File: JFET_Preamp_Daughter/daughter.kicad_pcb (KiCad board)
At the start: 2 copper layers, 80 x 120 mm, 90 parts, among them J101 Conn_01x02, J102 Conn_01x08_Socket, J201 XLR3, J301 XLR3, J401 XLR3, J501 XLR3, Q201 2SK209, Q202 2SK209, Q203 2SK209, Q301 2SK209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

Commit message: finish draft of mother/daughter sch and start routing, reconcile libraries and missing footprints
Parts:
- removed C201, C202, C203, C301, C302, C303, C401, C402, C403, C501, C502, C503: 220p, Capacitor_SMD:C_0603_1608Metric
- removed C204, C205, C304, C305, C404, C405, C504, C505: 10u, Capacitor_SMD:C_0805_2012Metric
- removed D102: LED, LED_SMD:LED_0603_1608Metric
- removed D201, D202, D301, D302, D401, D402, D501, D502: D_TVS, MMBZ27VALT1G:SOT95P237X111-3N
- removed J201, J301, J401, J501: XLR3, Connector_Audio:Jack_XLR_Neutrik_NC3FAH1_Horizontal
- removed Q201, Q202, Q203, Q301, Q302, Q303, Q401, Q402, Q403, Q501, Q502, Q503: 2SK209, Package_TO_SOT_SMD:SOT-23
- removed R201, R202, R301, R302, R401, R402, R501, R502: 6.81k, Resistor_SMD:R_0603_1608Metric
- removed R203, R303, R403, R503: 150, Resistor_SMD:R_0603_1608Metric
- removed R204, R205, R206, R207, R304, R305, R306, R307, R404, R405, R406, R407, R504, R505, R506, R507: 3M, Resistor_SMD:R_0603_1608Metric
- removed R208, R308, R408, R508: 470, Resistor_SMD:R_0603_1608Metric
- removed U102: TLV70012_SOT23-5, Package_TO_SOT_SMD:SOT-23-5
- added C107: 10u, Capacitor_SMD:C_0201_0603Metric, F.Cu at (61.4, 43.8)
- added C108: 10u, Capacitor_SMD:C_0201_0603Metric, F.Cu at (61.4, 45.5)
- added C109: 10u, Capacitor_SMD:C_0201_0603Metric, F.Cu at (61.4, 47.2)
- added C110: 10u, Capacitor_SMD:C_0201_0603Metric, F.Cu at (61.4, 49.0)
- added C111: 10u, Capacitor_SMD:C_0201_0603Metric, F.Cu at (63.8, 42.0)
- added C112: 10u, Capacitor_SMD:C_0201_0603Metric, F.Cu at (63.8, 43.8)
- added C113: 2.2u, Capacitor_SMD:C_0201_0603Metric, F.Cu at (63.8, 45.5)
- added J103: Conn_01x06, Connector_PinHeader_2.54mm:PinHeader_1x06_P2.54mm_Vertical, F.Cu at (44.0, 63.0)
- added R103: 0, Resistor_SMD:R_0603_1608Metric, F.Cu at (67.1, 47.4)
- C101: value 68u -> 10u; footprint Capacitor_SMD:CP_Elec_6.3x5.4 -> Capacitor_SMD:C_0201_0603Metric
- C102: value 1u -> 0.1u; footprint Capacitor_SMD:C_0603_1608Metric -> Capacitor_SMD:C_0201_0603Metric
- C103: value 100n -> 0.1u; footprint Capacitor_SMD:C_0603_1608Metric -> Capacitor_SMD:C_0201_0603Metric
- C104: value 1u -> 10u; footprint Capacitor_SMD:C_0603_1608Metric -> Capacitor_SMD:C_0201_0603Metric
- C105: value 100n -> 10u; footprint Capacitor_SMD:C_0603_1608Metric -> Capacitor_SMD:C_0201_0603Metric
- C106: value 2.2u -> 10u; footprint Capacitor_SMD:C_0603_1608Metric -> Capacitor_SMD:C_0201_0603Metric
- J101: value Conn_01x02 -> Conn_01x08_Socket; footprint Connector_PinHeader_2.54mm:PinHeader_1x02_P2.54mm_Vertical -> Connector_JST:JST_GH_BM08B-GHS-TBT_1x08-1MP_P1.25mm_Vertical
- J102: value Conn_01x08_Socket -> Conn_01x06; footprint Connector_PinHeader_2.54mm:PinHeader_1x08_P2.54mm_Vertical -> Connector_PinHeader_2.54mm:PinHeader_1x06_P2.54mm_Vertical
- R101: value 4.7k -> 1k
- R102: value 2.2k -> 0
- moved J102 109.5 mm to (44.0, 27.0), turned to 90 degrees
- moved J101 106.6 mm to (29.0, 44.5), turned to 90 degrees
- moved U101 87.6 mm to (49.5, 45.6), turned to 90 degrees
- moved R102 77.7 mm to (67.1, 44.9), turned to 0 degrees
- moved C106 75.2 mm to (61.4, 42.0), turned to 0 degrees
- moved C104 74.8 mm to (58.9, 47.2), turned to 0 degrees
- moved C105 71.1 mm to (58.9, 49.0)
- moved C101 70.1 mm to (58.9, 42.0), turned to 0 degrees
- moved R101 68.8 mm to (67.1, 42.4), turned to 0 degrees
- moved D101 65.2 mm to (71.1, 42.4), turned to 0 degrees
- moved C102 64.7 mm to (58.9, 43.8), turned to 0 degrees
- moved C103 60.9 mm to (58.9, 45.5), turned to 0 degrees
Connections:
- C101 pad 1: +24V -> +3.3V
- C102 pad 1: +24V -> +3.3V
- C103 pad 1: +24V -> +3.3V
- C104 pad 1: Net-(U101-LDO) -> +3.3V
- C105 pad 1: GND -> /CH1_HOT
- C105 pad 2: Net-(U101-Mic_Bias) -> Net-(U101-VINL1/VIN1P)
- C106 pad 1: Net-(U101-VREF) -> /CH1_COLD
- C106 pad 2: GND -> Net-(U101-VINL2/VIN1M)
- J101 pad 1: +24V -> +3.3V
- J102 pad 1: +3.3V -> /CH3_COLD
- J102 pad 2: GND -> /CH4_COLD
- J102 pad 3: /MCLK -> GND
- J102 pad 4: /I2S_BCK -> GND
- J102 pad 5: /I2S_LRCK -> /CH3_HOT
- J102 pad 6: /I2S_DOUT -> /CH4_HOT
- R101 pad 2: +24V -> /I2S_DOUT
- R102 pad 1: Net-(D102-A) -> GND
- R102 pad 2: /I2S_DOUT -> GND
- U101 pad 1: /CH1_COLD -> Net-(U101-VINL2/VIN1M)
- U101 pad 11: +1.8V -> unconnected-(U101-LDO-Pad11)
- U101 pad 14: +1.8V -> +3.3V
- U101 pad 2: /CH2_COLD -> Net-(U101-VINR2/VIN2M)
- U101 pad 27: /CH3_COLD -> Net-(U101-VINL4/VIN4M)
- U101 pad 28: /CH4_COLD -> Net-(U101-VINR4/VIN3M)
- U101 pad 29: /CH3_HOT -> Net-(U101-VINL3/VIN4P)
- U101 pad 3: /CH1_HOT -> Net-(U101-VINL1/VIN1P)
- U101 pad 30: /CH4_HOT -> Net-(U101-VINR3/VIN3P)
- U101 pad 4: /CH2_HOT -> Net-(U101-VINR1/VIN2P)
- U101 pad 5: Net-(U101-Mic_Bias) -> unconnected-(U101-Mic_Bias-Pad5)
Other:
- board size 80 x 120 mm -> 50 x 40 mm
- board text removed: "+24V"
- board text removed: "@cakemoji"
- board text removed: "COMM STATUS"
- board text removed: "Ch.1"
- board text removed: "Ch.2"
- board text removed: "Ch.3"
- board text removed: "Ch.4"
- board text removed: "Designed by Lucas Samaniego reference: zachpoff.com/resources/alex-rice-preamplifier"
- board text removed: "J102 1. +3.3V 2. GND 3. MCLK 4. I2S_BCK 5. I2S_LRCK 6. I2S_DOUT 7. I2S_SDA 8. I2S_SCL"
- board text removed: "JFET Preamp with ADC PCB By Lucas Samaniego"
- board text removed: "PWR STATUS"

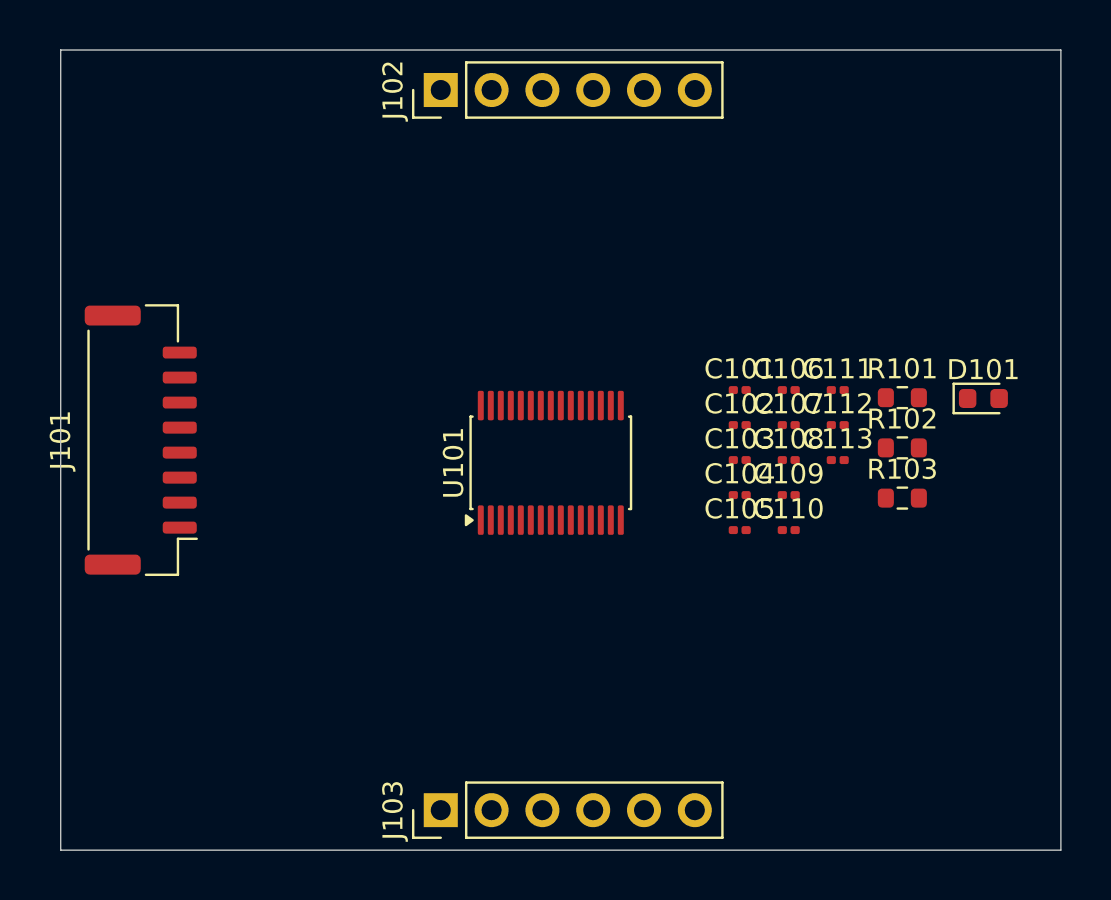
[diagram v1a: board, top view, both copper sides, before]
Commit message: finish routing daughterboard and fix 0 ohm resistor on AGND/DGND for schematic
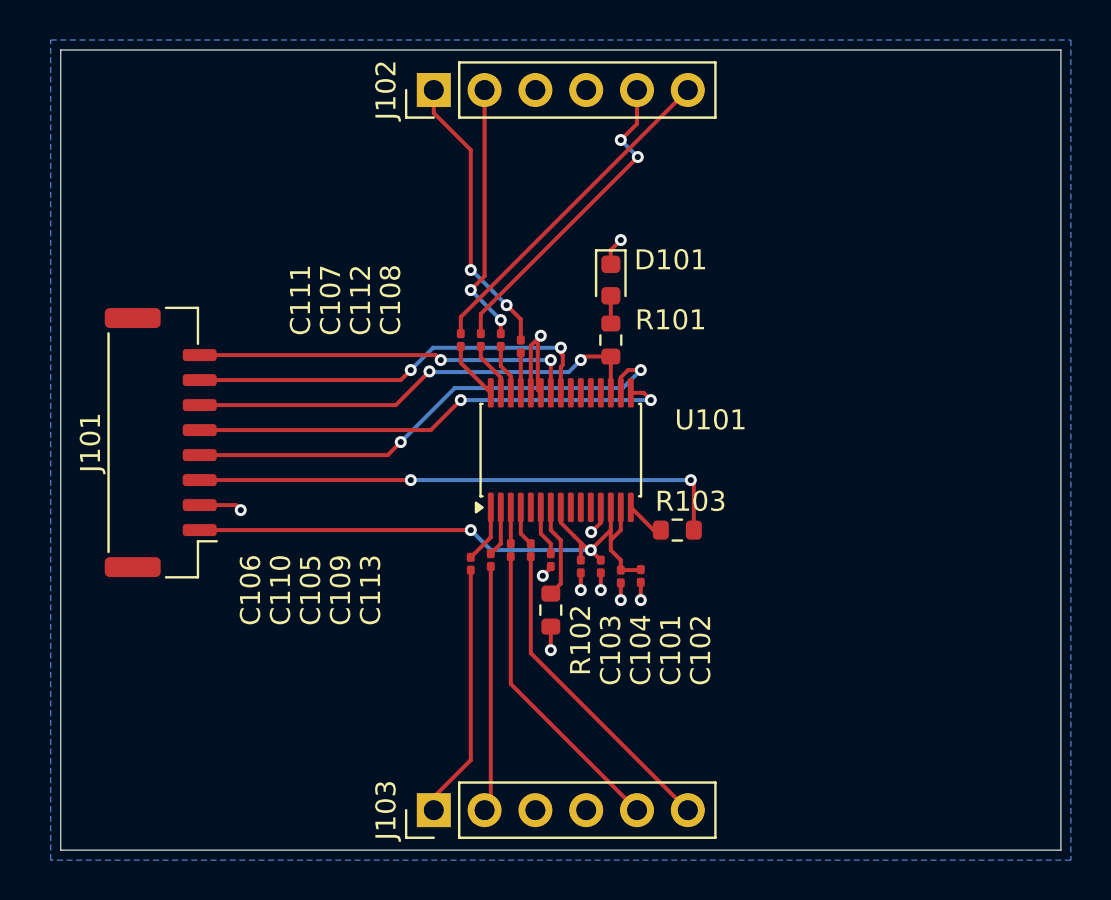
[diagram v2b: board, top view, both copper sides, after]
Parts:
- moved D101 19.5 mm to (52.5, 36.5), turned to -90 degrees
- moved R102 19.4 mm to (49.5, 53.0), turned to -90 degrees
- moved C111 19.0 mm to (45.0, 39.5), turned to -90 degrees
- moved C106 18.1 mm to (45.5, 50.7), turned to 90 degrees
- moved C112 17.4 mm to (47.0, 39.5), turned to -90 degrees
- moved C107 16.0 mm to (46.0, 39.5), turned to -90 degrees
- moved C113 15.2 mm to (49.5, 50.5), turned to -90 degrees
- moved C110 15.0 mm to (46.5, 50.5), turned to 90 degrees
- moved R101 14.9 mm to (52.5, 39.5), turned to -90 degrees
- moved C108 14.5 mm to (48.0, 39.8), turned to -90 degrees
- moved C109 13.2 mm to (48.5, 50.0), turned to 90 degrees
- moved C105 11.5 mm to (47.5, 50.0), turned to 90 degrees
- moved R103 11.4 mm to (55.8, 49.0)
- moved C101 11.1 mm to (53.0, 51.3), turned to -90 degrees
- moved C103 9.56 mm to (51.0, 50.8), turned to -90 degrees
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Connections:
- R102 pad 1: GND -> Net-(U101-AGND)
- U101 pad 7: GND -> Net-(U101-AGND)
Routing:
- net +3.3V: track 0.00 -> 32.0 mm, vias 0 -> 2
- net Net-(J101-Pin_3): track 0.00 -> 27.1 mm, vias 0 -> 2
- net /I2S_BCK: track 0.00 -> 25.7 mm, vias 0 -> 2
- net /I2S_LRCK: track 0.00 -> 24.3 mm, vias 0 -> 2
- net /I2S_DOUT: track 0.00 -> 23.4 mm, vias 0 -> 2
- net /I2S_SDA: track 0.00 -> 21.1 mm, vias 0 -> 2
- net /I2S_SCL: track 0.00 -> 19.3 mm, vias 0 -> 2
- net /CH4_HOT: track 0.00 -> 16.9 mm
- net GND: track 0.00 -> 16.3 mm, vias 0 -> 10
- net /CH3_HOT: track 0.00 -> 16.1 mm, vias 0 -> 2
- net /CH2_HOT: track 0.00 -> 15.9 mm
- net /CH1_HOT: track 0.00 -> 15.3 mm
- net /CH3_COLD: track 0.00 -> 14.3 mm, vias 0 -> 2
- net /CH4_COLD: track 0.00 -> 13.1 mm, vias 0 -> 2
- net /CH1_COLD: track 0.00 -> 12.8 mm
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- added copper zone on B.Cu, net GND

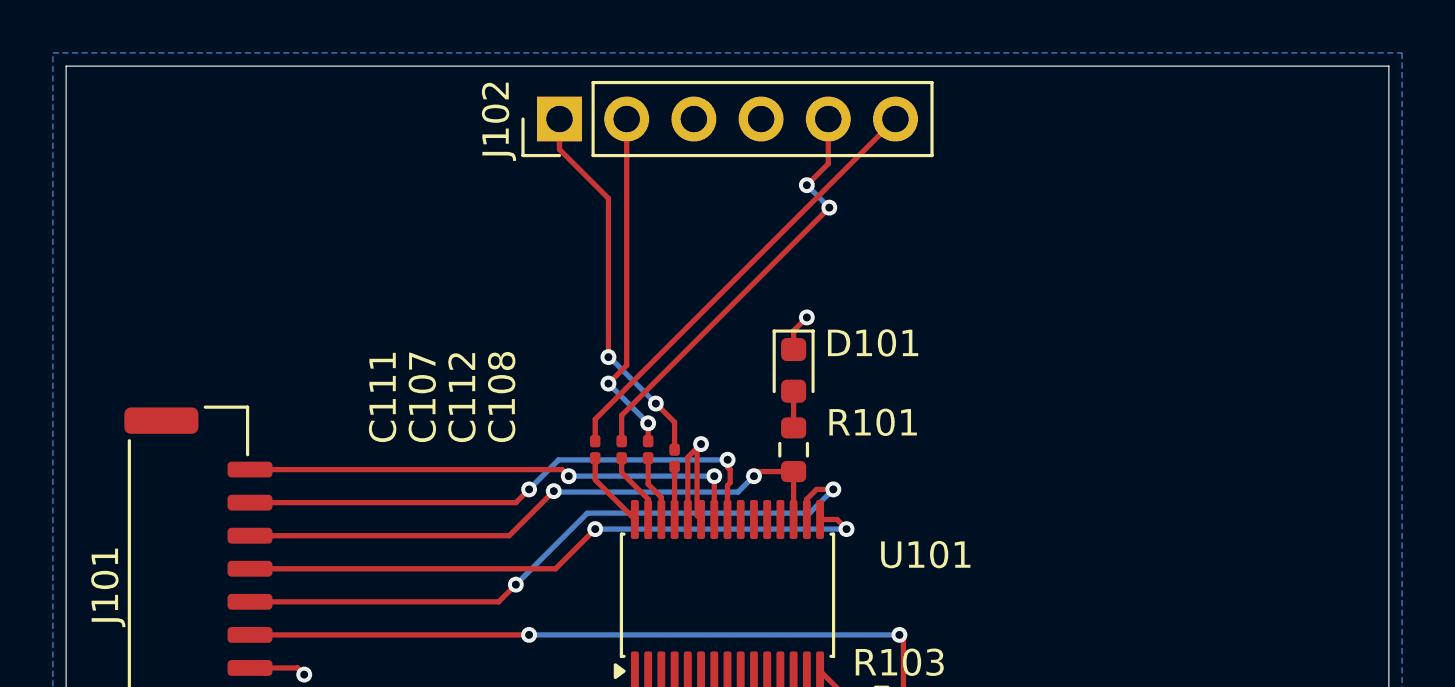
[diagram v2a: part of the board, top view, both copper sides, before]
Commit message: add silkscreen to pcb daughterboard, possibly final pending review
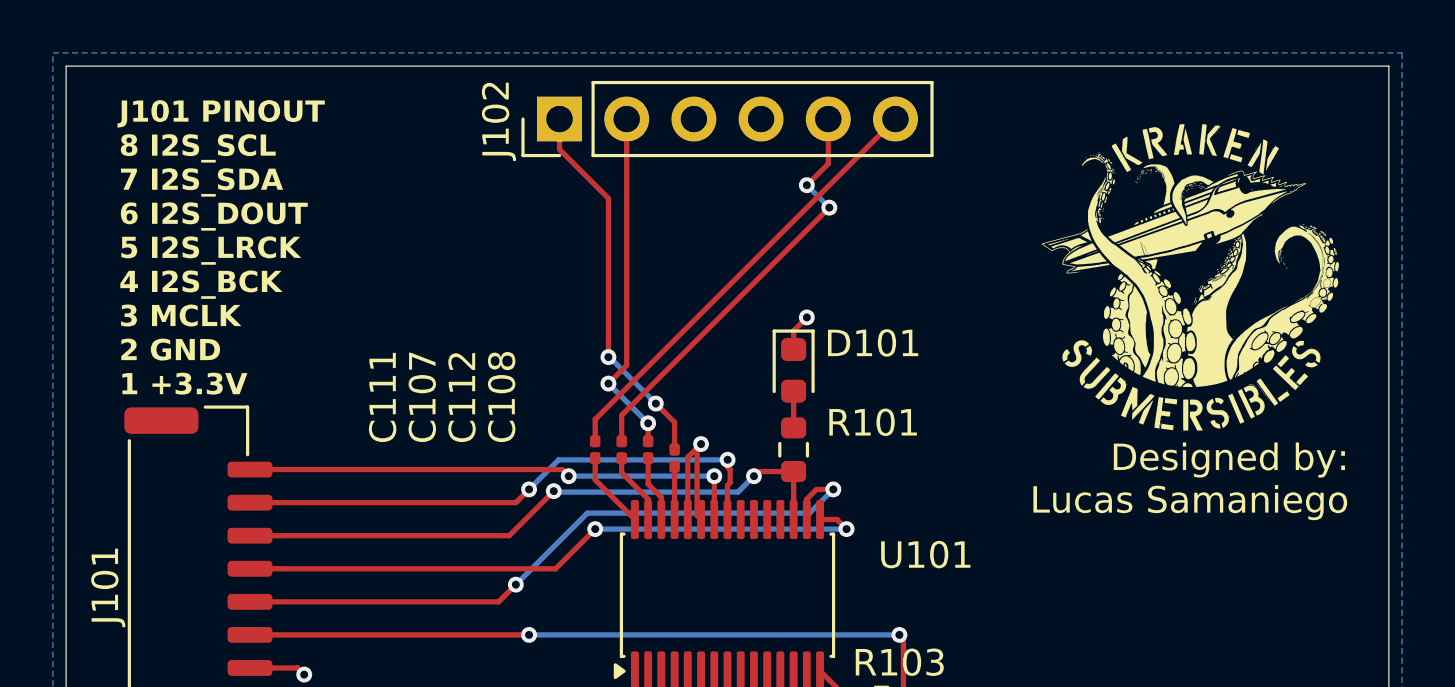
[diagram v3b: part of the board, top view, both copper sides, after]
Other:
- board text added: "Designed by: Lucas Samaniego"
- board text added: "J101 PINOUT 8 I2S_SCL 7 I2S_SDA 6 I2S_DOUT 5 I2S_LRCK 4 I2S_BCK 3 MCLK 2 GND 1 +3.3V"
